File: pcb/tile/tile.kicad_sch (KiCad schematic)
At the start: 21 parts, among them IC1 THVD1420DR, J1 LED Strip, J2 UPDI, J3 5555140-2, J4 5555140-2, J5 12V, U1 ATtiny3224-X

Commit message: Small tweaks
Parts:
- added R3: 120 Ohm, Resistor_SMD:R_0805_2012Metric_Pad1.20x1.40mm_HandSolder, symbol Device:R_US
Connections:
- net TRCV-A: now also R3.1
- net TRCV-B: now also R3.2
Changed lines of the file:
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@@
+	)
+	(junction
+		(at 167.64 102.87)
+		(diameter 0)
+		(color 0 0 0 0)
 	)
 	(junction
@@
 	)
 	(junction
+		(at 167.64 81.28)
+		(diameter 0)
+		(color 0 0 0 0)
+	)
+	(junction
 		(at 45.72 50.8)
 		(diameter 0)
@@
 	(wire
 		(pts
-			(xy 168.91 81.28) (xy 165.1 81.28)
+			(xy 168.91 81.28) (xy 167.64 81.28)
 		)
 		(stroke
@@
 	(wire
 		(pts
+			(xy 167.64 96.52) (xy 167.64 102.87)
+		)
+		(stroke
+			(width 0)
+			(type default)
+		)
+	)
+	(wire
+		(pts
 			(xy 191.77 100.33) (xy 195.58 100.33)
 		)
@@
 	(wire
 		(pts
+			(xy 167.64 81.28) (xy 167.64 88.9)
+		)
+		(stroke
+			(width 0)
+			(type default)
+		)
+	)
+	(wire
+		(pts
 			(xy 107.95 148.59) (xy 107.95 157.48)
 		)
@@
 	(wire
 		(pts
+			(xy 167.64 102.87) (xy 168.91 102.87)
+		)
+		(stroke
+			(width 0)
+			(type default)
+		)
+	)
+	(wire
+		(pts
 			(xy 180.34 36.83) (xy 191.77 36.83)
 		)
@@
 	(wire
 		(pts
-			(xy 162.56 102.87) (xy 168.91 102.87)
+			(xy 162.56 102.87) (xy 167.64 102.87)
 		)
 		(stroke
@@
 		(pts
 			(xy 148.59 30.48) (xy 148.59 34.29)
+		)
+		(stroke
+			(width 0)
+			(type default)
+		)
+	)
+	(wire
+		(pts
+			(xy 167.64 81.28) (xy 165.1 81.28)
 		)
 		(stroke
@@
 					(unit 1)
 				)
+			)
+		)
+	)
+	(symbol
+		(lib_id "Device:R_US")
+		(at 167.64 92.71 0)
+		(unit 1)
+		(exclude_from_sim no)
+		(in_bom yes)
+		(on_board yes)
+		(dnp no)
+		(fields_autoplaced yes)
+		(property "Reference" "R3"
+			(at 170.18 91.4399 0)
+			(effects
+				(font
+					(size 1.27 1.27)
+				)
+				(justify left)
+			)
+		)
+		(property "Value" "120 Ohm"
+			(at 170.18 93.9799 0)
+			(effects
+				(font
+					(size 1.27 1.27)
+				)
+				(justify left)
+			)
+		)
+		(property "Footprint" "Resistor_SMD:R_0805_2012Metric_Pad1.20x1.40mm_HandSolder"
+			(at 168.656 92.964 90)
+			(effects
+				(font
+					(size 1.27 1.27)
+				)
+				(hide yes)
+			)
+		)
+		(property "Datasheet" "~"
+			(at 167.64 92.71 0)
+			(effects
+				(font
+					(size 1.27 1.27)
+				)
+				(hide yes)
+			)
+		)
+		(property "Description" "Resistor, US symbol"
+			(at 167.64 92.71 0)
+			(effects
+				(font
+					(size 1.27 1.27)
+				)
+				(hide yes)
+			)
+		)
+		(pin "2"
+		)
+		(pin "1"
+		)
+		(instances
+			(project "tile"
+				(path "/68eea85a-4a75-40a0-9423-1988556e9fbf"
+					(reference "R3")
+					(unit 1)
+				)

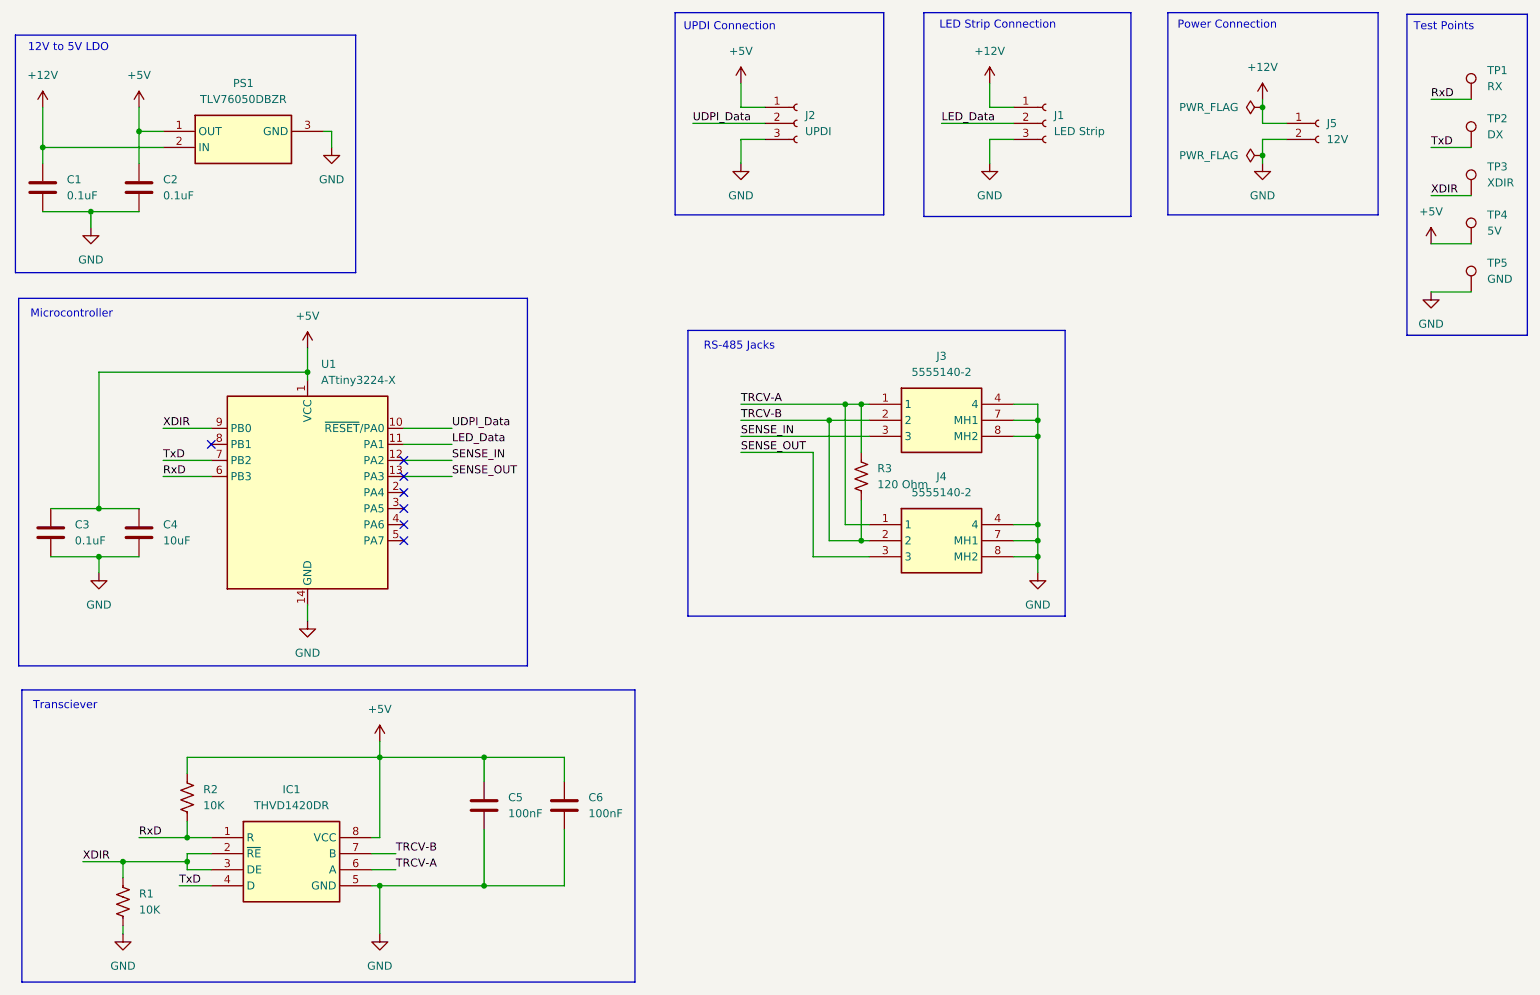
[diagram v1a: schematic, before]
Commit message: Updated version of the tile that only uses on RJ45 jack vs two RJ12 jacks
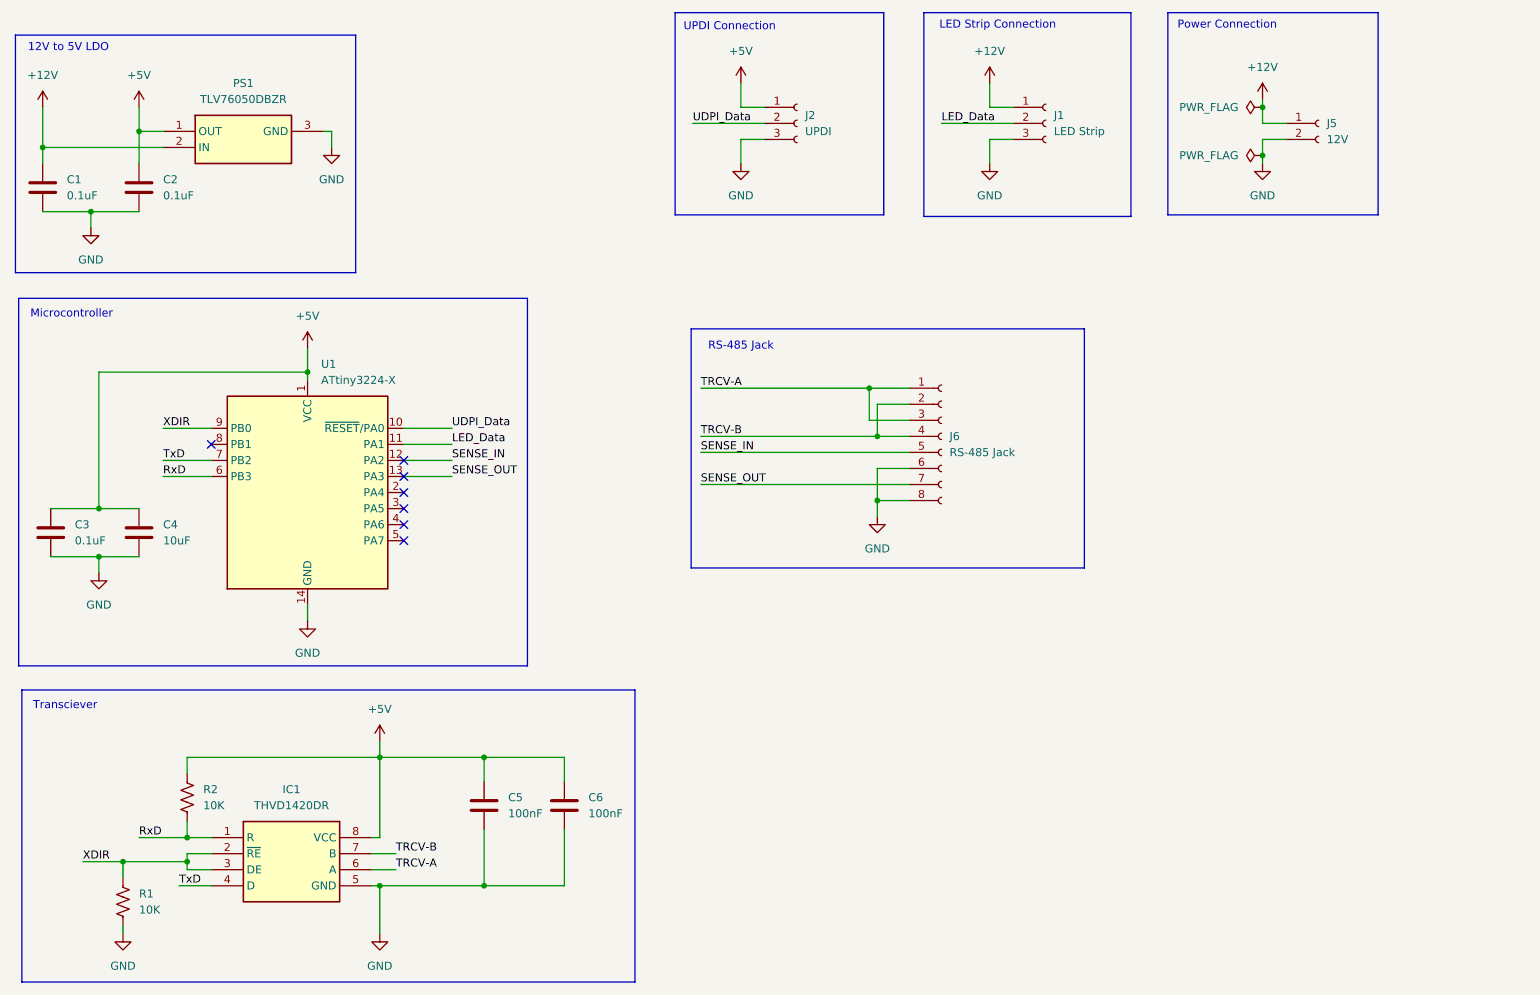
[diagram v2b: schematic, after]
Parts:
- removed J3, J4: 5555140-2, 5555140-2:55551402, symbol 5555140-2:5555140-2
- removed R3: 120 Ohm, Resistor_SMD:R_0805_2012Metric_Pad1.20x1.40mm_HandSolder, symbol Device:R_US
- removed TP1: RX, TestPoint:TestPoint_THTPad_D1.5mm_Drill0.7mm, symbol Connector:TestPoint
- removed TP2: DX, TestPoint:TestPoint_THTPad_D1.5mm_Drill0.7mm, symbol Connector:TestPoint
- removed TP3: XDIR, TestPoint:TestPoint_THTPad_D1.5mm_Drill0.7mm, symbol Connector:TestPoint
- removed TP4: 5V, TestPoint:TestPoint_THTPad_D1.5mm_Drill0.7mm, symbol Connector:TestPoint
- removed TP5: GND, TestPoint:TestPoint_THTPad_D1.5mm_Drill0.7mm, symbol Connector:TestPoint
- added J6: RS-485 Jack, Garth:6P6C RA RJ45 Jack, symbol Connector:Conn_01x08_Socket
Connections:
- net GND: now also J6.6 (Pin_6), J6.8 (Pin_8)
- net SENSE_IN: now also J6.5 (Pin_5)
- net SENSE_OUT: now also J6.7 (Pin_7)
- net TRCV-A: now also J6.1 (Pin_1), J6.3 (Pin_3)
- net TRCV-B: now also J6.2 (Pin_2), J6.4 (Pin_4)
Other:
- note added: "RS-485 Jack"
- note removed: "RS-485 Jacks"
- note removed: "Test Points"

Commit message: Committing PCB changes before swaping out some components
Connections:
- no-connect marks 7 -> 5

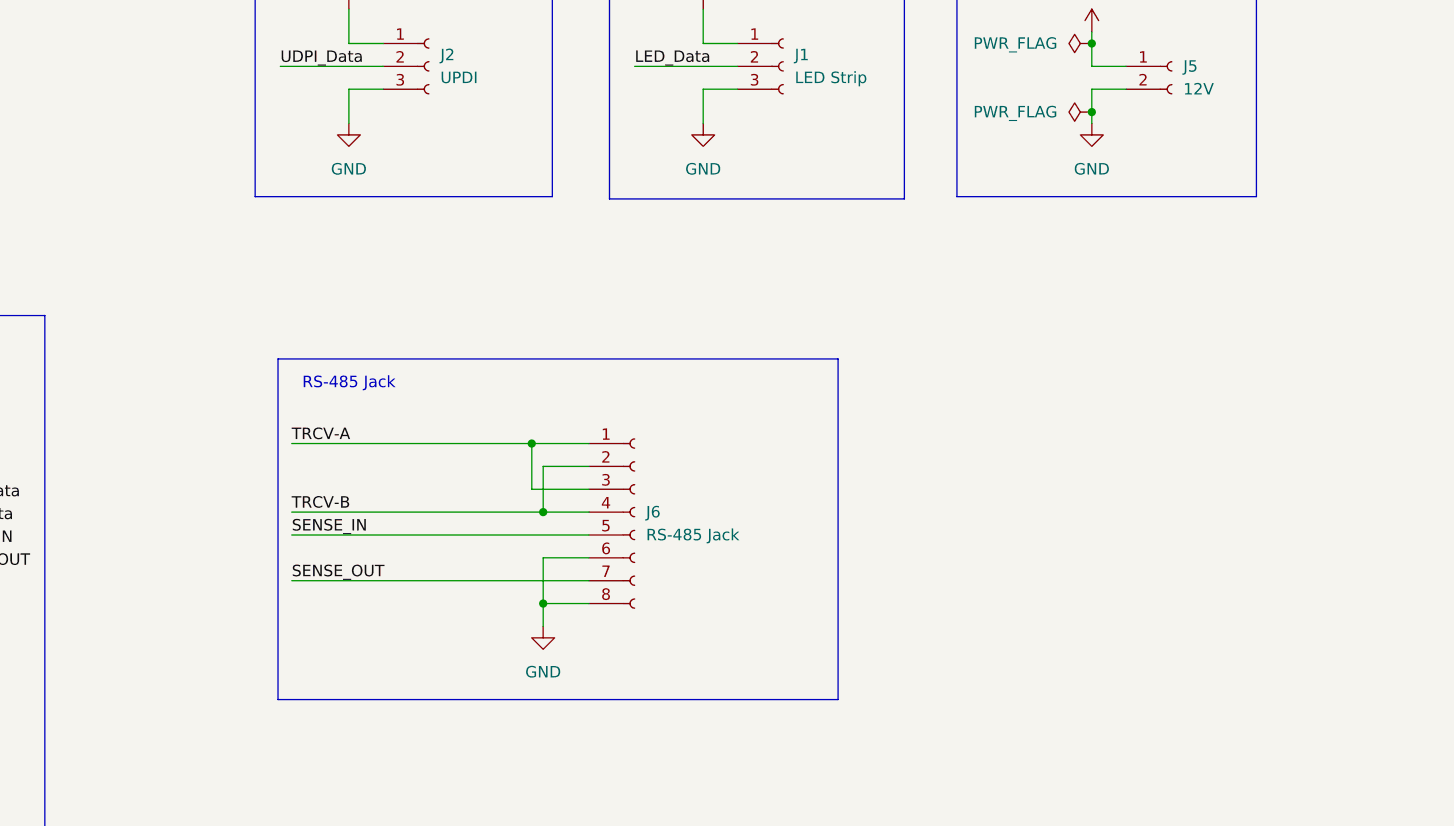
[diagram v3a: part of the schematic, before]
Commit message: Additon of second power jack, plus notes/todos for things that need updating
Checkpointing here since this is what the last fab got and I want to be able to come back to it
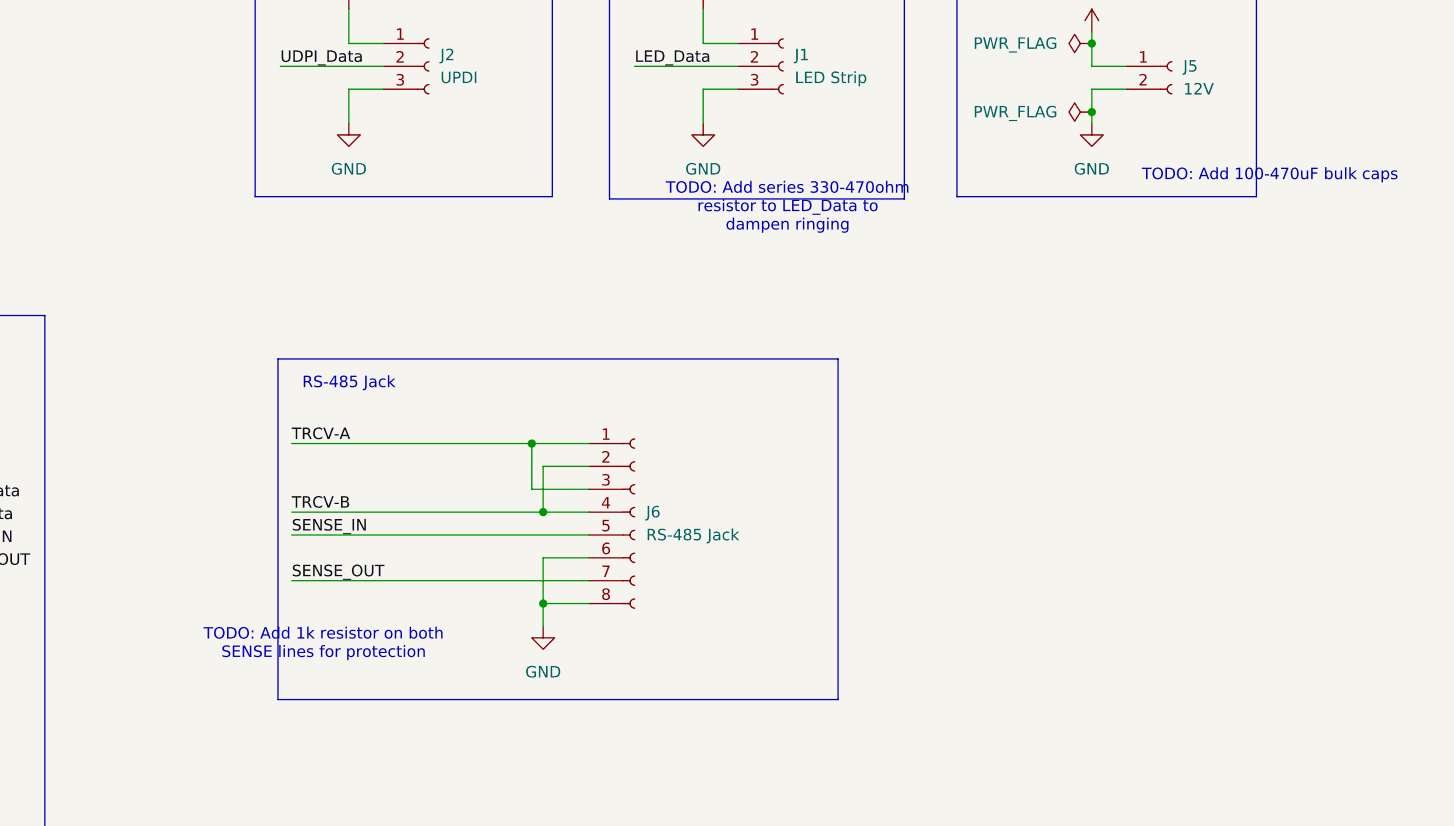
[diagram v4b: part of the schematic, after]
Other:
- note added: "TODO: Add 100-470uF bulk caps"
- note added: "TODO: Add 1k resistor on both SENSE lines for protection"
- note added: "TODO: Add series 330-470ohm resistor to LED_Data to dampen ringing"
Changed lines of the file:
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@@
+		)
+	)
+	(text "TODO: Add series 330-470ohm \nresistor to LED_Data to \ndampen ringing"
+		(exclude_from_sim no)
+		(at 197.358 52.578 0)
+		(effects
+			(font
+				(size 1.27 1.27)
+			)
+		)
+	)
+	(text "TODO: Add 1k resistor on both \nSENSE lines for protection"
+		(exclude_from_sim no)
+		(at 145.796 101.092 0)
+		(effects
+			(font
+				(size 1.27 1.27)
+			)
 		)
 	)
@@
 		(effects
 			(font
+				(size 1.27 1.27)
+			)
+		)
+	)
+	(text "TODO: Add 100-470uF bulk caps"
+		(exclude_from_sim no)
+		(at 250.952 49.022 0)
+		(effects
+			(font
